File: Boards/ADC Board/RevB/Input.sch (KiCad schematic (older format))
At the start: 3 parts

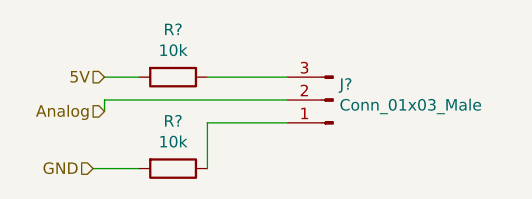
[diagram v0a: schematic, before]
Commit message: Began footprint associations for rev b
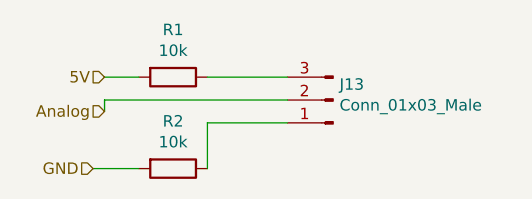
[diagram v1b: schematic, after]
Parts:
- J13: renamed from J?; footprint (none) -> Connector_PinHeader_2.54mm:PinHeader_1x03_P2.54mm_Vertical
- gave numbers to parts that had none: 2
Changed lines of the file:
@@
 $Descr A4 11693 8268
 encoding utf-8
-Sheet 14 13
+Sheet 5 13
 Title ""
 Date ""
@@
 Analog
 $Comp
-L Device:R R?
+L Device:R R1
 U 1 1 62327307
 P 2050 1400
-AR Path="/62325883/62325A7E/62327307" Ref="R?"  Part="1"
-AR Path="/62325883/6232E183/62327307" Ref="R?"  Part="1"
-AR Path="/62325883/6232E335/62327307" Ref="R?"  Part="1"
-AR Path="/62325883/6232E4F3/62327307" Ref="R?"  Part="1"
-AR Path="/62325883/6232EF2C/62327307" Ref="R?"  Part="1"
-AR Path="/62325883/6232EF31/62327307" Ref="R?"  Part="1"
-AR Path="/62325883/6232EF36/62327307" Ref="R?"  Part="1"
-AR Path="/62325883/6232EF3B/62327307" Ref="R?"  Part="1"
-F 0 "R?" V 1843 1400 50  0000 C CNN
+AR Path="/62325883/62325A7E/62327307" Ref="R1"  Part="1"
+AR Path="/62325883/6232E183/62327307" Ref="R3"  Part="1"
+AR Path="/62325883/6232E335/62327307" Ref="R5"  Part="1"
+AR Path="/62325883/6232E4F3/62327307" Ref="R7"  Part="1"
+AR Path="/62325883/6232EF2C/62327307" Ref="R10"  Part="1"
+AR Path="/62325883/6232EF31/62327307" Ref="R12"  Part="1"
+AR Path="/62325883/6232EF36/62327307" Ref="R14"  Part="1"
+AR Path="/62325883/6232EF3B/62327307" Ref="R16"  Part="1"
+F 0 "R1" V 1843 1400 50  0000 C CNN
 F 1 "10k" V 1934 1400 50  0000 C CNN
 F 2 "" V 1980 1400 50  0001 C CNN
@@
 $EndComp
 $Comp
-L Device:R R?
+L Device:R R2
 U 1 1 6232834A
 P 2050 1800
-AR Path="/62325883/62325A7E/6232834A" Ref="R?"  Part="1"
-AR Path="/62325883/6232E183/6232834A" Ref="R?"  Part="1"
-AR Path="/62325883/6232E335/6232834A" Ref="R?"  Part="1"
-AR Path="/62325883/6232E4F3/6232834A" Ref="R?"  Part="1"
-AR Path="/62325883/6232EF2C/6232834A" Ref="R?"  Part="1"
-AR Path="/62325883/6232EF31/6232834A" Ref="R?"  Part="1"
-AR Path="/62325883/6232EF36/6232834A" Ref="R?"  Part="1"
-AR Path="/62325883/6232EF3B/6232834A" Ref="R?"  Part="1"
-F 0 "R?" V 1843 1800 50  0000 C CNN
+AR Path="/62325883/62325A7E/6232834A" Ref="R2"  Part="1"
+AR Path="/62325883/6232E183/6232834A" Ref="R4"  Part="1"
+AR Path="/62325883/6232E335/6232834A" Ref="R6"  Part="1"
+AR Path="/62325883/6232E4F3/6232834A" Ref="R8"  Part="1"
+AR Path="/62325883/6232EF2C/6232834A" Ref="R11"  Part="1"
+AR Path="/62325883/6232EF31/6232834A" Ref="R13"  Part="1"
+AR Path="/62325883/6232EF36/6232834A" Ref="R15"  Part="1"
+AR Path="/62325883/6232EF3B/6232834A" Ref="R17"  Part="1"
+F 0 "R2" V 1843 1800 50  0000 C CNN
 F 1 "10k" V 1934 1800 50  0000 C CNN
 F 2 "" V 1980 1800 50  0001 C CNN
@@
 	1900 1400 1750 1400
 $Comp
-L Connector:Conn_01x03_Male J?
+L Connector:Conn_01x03_Male J13
 U 1 1 62328697
 P 2750 1500
-AR Path="/62325883/62325A7E/62328697" Ref="J?"  Part="1"
-AR Path="/62325883/6232E183/62328697" Ref="J?"  Part="1"
-AR Path="/62325883/6232E335/62328697" Ref="J?"  Part="1"
-AR Path="/62325883/6232E4F3/62328697" Ref="J?"  Part="1"
-AR Path="/62325883/6232EF2C/62328697" Ref="J?"  Part="1"
-AR Path="/62325883/6232EF31/62328697" Ref="J?"  Part="1"
-AR Path="/62325883/6232EF36/62328697" Ref="J?"  Part="1"
-AR Path="/62325883/6232EF3B/62328697" Ref="J?"  Part="1"
-F 0 "J?" H 2722 1432 50  0000 R CNN
+AR Path="/62325883/62325A7E/62328697" Ref="J13"  Part="1"
+AR Path="/62325883/6232E183/62328697" Ref="J14"  Part="1"
+AR Path="/62325883/6232E335/62328697" Ref="J15"  Part="1"
+AR Path="/62325883/6232E4F3/62328697" Ref="J16"  Part="1"
+AR Path="/62325883/6232EF2C/62328697" Ref="J17"  Part="1"
+AR Path="/62325883/6232EF31/62328697" Ref="J18"  Part="1"
+AR Path="/62325883/6232EF36/62328697" Ref="J19"  Part="1"
+AR Path="/62325883/6232EF3B/62328697" Ref="J20"  Part="1"
+F 0 "J13" H 2722 1432 50  0000 R CNN
 F 1 "Conn_01x03_Male" H 2722 1523 50  0000 R CNN
-F 2 "" H 2750 1500 50  0001 C CNN
+F 2 "Connector_PinHeader_2.54mm:PinHeader_1x03_P2.54mm_Vertical" H 2750 1500 50  0001 C CNN
 F 3 "~" H 2750 1500 50  0001 C CNN
 	1    2750 1500

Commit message: Created PCB for Rev B
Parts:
- R1, R2: footprint (none) -> Resistor_SMD:R_0603_1608Metric
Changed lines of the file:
@@
 $Descr A4 11693 8268
 encoding utf-8
-Sheet 5 13
+Sheet 11 13
 Title ""
 Date ""
@@
 AR Path="/62325883/6232EF36/62327307" Ref="R14"  Part="1"
 AR Path="/62325883/6232EF3B/62327307" Ref="R16"  Part="1"
-F 0 "R1" V 1843 1400 50  0000 C CNN
+F 0 "R16" V 1843 1400 50  0000 C CNN
 F 1 "10k" V 1934 1400 50  0000 C CNN
-F 2 "" V 1980 1400 50  0001 C CNN
+F 2 "Resistor_SMD:R_0603_1608Metric" V 1980 1400 50  0001 C CNN
 F 3 "~" H 2050 1400 50  0001 C CNN
 	1    2050 1400
@@
 AR Path="/62325883/6232EF36/6232834A" Ref="R15"  Part="1"
 AR Path="/62325883/6232EF3B/6232834A" Ref="R17"  Part="1"
-F 0 "R2" V 1843 1800 50  0000 C CNN
+F 0 "R17" V 1843 1800 50  0000 C CNN
 F 1 "10k" V 1934 1800 50  0000 C CNN
-F 2 "" V 1980 1800 50  0001 C CNN
+F 2 "Resistor_SMD:R_0603_1608Metric" V 1980 1800 50  0001 C CNN
 F 3 "~" H 2050 1800 50  0001 C CNN
 	1    2050 1800
@@
 AR Path="/62325883/6232EF36/62328697" Ref="J19"  Part="1"
 AR Path="/62325883/6232EF3B/62328697" Ref="J20"  Part="1"
-F 0 "J13" H 2722 1432 50  0000 R CNN
+F 0 "J20" H 2722 1432 50  0000 R CNN
 F 1 "Conn_01x03_Male" H 2722 1523 50  0000 R CNN
 F 2 "Connector_PinHeader_2.54mm:PinHeader_1x03_P2.54mm_Vertical" H 2750 1500 50  0001 C CNN

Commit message: Continued making RevB PCB
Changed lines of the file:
@@
 $Descr A4 11693 8268
 encoding utf-8
-Sheet 11 13
+Sheet 8 13
 Title ""
 Date ""
@@
 AR Path="/62325883/6232EF36/62327307" Ref="R14"  Part="1"
 AR Path="/62325883/6232EF3B/62327307" Ref="R16"  Part="1"
-F 0 "R16" V 1843 1400 50  0000 C CNN
+F 0 "R7" V 1843 1400 50  0000 C CNN
 F 1 "10k" V 1934 1400 50  0000 C CNN
 F 2 "Resistor_SMD:R_0603_1608Metric" V 1980 1400 50  0001 C CNN
@@
 AR Path="/62325883/6232EF36/6232834A" Ref="R15"  Part="1"
 AR Path="/62325883/6232EF3B/6232834A" Ref="R17"  Part="1"
-F 0 "R17" V 1843 1800 50  0000 C CNN
+F 0 "R8" V 1843 1800 50  0000 C CNN
 F 1 "10k" V 1934 1800 50  0000 C CNN
 F 2 "Resistor_SMD:R_0603_1608Metric" V 1980 1800 50  0001 C CNN
@@
 AR Path="/62325883/6232EF36/62328697" Ref="J19"  Part="1"
 AR Path="/62325883/6232EF3B/62328697" Ref="J20"  Part="1"
-F 0 "J20" H 2722 1432 50  0000 R CNN
+F 0 "J16" H 2722 1432 50  0000 R CNN
 F 1 "Conn_01x03_Male" H 2722 1523 50  0000 R CNN
 F 2 "Connector_PinHeader_2.54mm:PinHeader_1x03_P2.54mm_Vertical" H 2750 1500 50  0001 C CNN
